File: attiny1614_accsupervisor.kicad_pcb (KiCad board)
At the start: 2 copper layers, 58 x 58 mm, 34 parts, among them J1 VXO7803-500-M-TR, J2 MSTBA_2,5_3-G, J3 Conn_01x02, J4 Conn_02x20_Odd_Even, J5 AVR-UPDI-6, K1 JSM1-12V-5, Q1 BC817, Q2 BC817, Q3 BC817, Q4 BSS84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

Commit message: r01 gerber generated
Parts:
- moved Q3 77.1 mm to (222.5, 91.5)
- moved R5 74.8 mm to (225.5, 89.5), turned to 90 degrees
- moved R3 73.2 mm to (214.0, 90.0), turned to 90 degrees
- moved R7 71.9 mm to (223.0, 84.5)
- moved R8 71.1 mm to (218.5, 72.5), turned to 90 degrees
- moved R10 66.6 mm to (218.5, 78.0), turned to 90 degrees
- moved R2 65.7 mm to (214.0, 79.5), turned to 270 degrees
- moved R9 59.5 mm to (218.5, 86.0), turned to 90 degrees
- moved R11 57.8 mm to (218.5, 91.5), turned to 90 degrees
- moved Q5 52.2 mm to (222.5, 87.5)
- moved F1 19.7 mm to (226.0, 52.5), turned to 180 degrees
- moved R12 17.2 mm to (240.5, 92.0)
- moved R13 17.2 mm to (243.5, 92.0)
- moved R14 17.2 mm to (234.5, 92.0)
- moved R15 17.2 mm to (237.5, 92.0)
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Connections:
- U1 pad 12: (no net) -> /ADC_ON
- U1 pad 4: /ADC1_VIN -> /ADC2_ACC
- U1 pad 5: /ADC2_ACC -> /ADC1_VIN
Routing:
- net /12V: track 0.00 -> 76.9 mm
- net /AVR_TX: track 0.00 -> 52.0 mm
- net /AVR_RX: track 0.00 -> 44.0 mm
- net /ADC1_VIN: track 0.00 -> 29.5 mm
- net /RLY_ON: track 0.00 -> 26.3 mm
- net /3V3: track 0.00 -> 24.5 mm
- net /ACC: track 0.00 -> 24.1 mm
- net /JST_TX: track 0.00 -> 21.2 mm
- net /12V_IN: track 0.00 -> 20.3 mm
- net /ADC2_ACC: track 0.00 -> 17.7 mm
- net /UPDI_DATA: track 0.00 -> 16.0 mm
- net Net-(D1-Pad2): track 0.00 -> 15.9 mm
- net /ADC_ON: track 0.00 -> 12.8 mm
- net /JST_RX: track 0.00 -> 10.9 mm
- net Net-(Q3-Pad1): track 0.00 -> 7.90 mm
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- added copper zone on B.Cu, net GND
- added copper zone on F.Cu, net GND

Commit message: Layout done
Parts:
- added G***: LOGO, attiny1614_accsupervisor:Doge, F.Cu at (230.0, 69.0)
- moved R13 48.4 mm to (197.5, 77.0), turned to 0 degrees
- moved J4 48.3 mm to (194.9, 99.2), turned to 90 degrees
- moved R14 39.1 mm to (197.5, 79.5), turned to 0 degrees
- moved R12 33.5 mm to (207.0, 92.0)
- moved R15 33.0 mm to (204.5, 92.0)
- moved U1 7.76 mm to (205.0, 81.5)
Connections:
- U1 pad 11: /RLY_ON -> /ADC1_VIN
- U1 pad 12: /ADC_ON -> /ADC2_ACC
- U1 pad 13: (no net) -> /ADC_ON
- U1 pad 4: /ADC2_ACC -> (no net)
- U1 pad 5: /ADC1_VIN -> (no net)
- U1 pad 8: (no net) -> /RLY_ON
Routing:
- net /AVR_TX: track 52.0 -> 19.1 mm
- net /AVR_RX: track 44.0 -> 16.7 mm
- net /RLY_ON: track 26.3 -> 9.89 mm
- net /JST_TX: track 21.2 -> 35.1 mm
- net /ADC1_VIN: track 29.5 -> 18.0 mm
- net /UPDI_DATA: track 16.0 -> 24.4 mm
- net /ADC2_ACC: track 17.7 -> 23.0 mm
- net /JST_RX: track 10.9 -> 5.86 mm
- net /3V3: track 24.5 -> 29.5 mm
- net /ADC_ON: track 12.8 -> 15.4 mm
- net GND: vias 90 -> 116
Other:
- board text added: "ACC Supervisor ATTINY r01 (c) 2020, Jason Kwon"

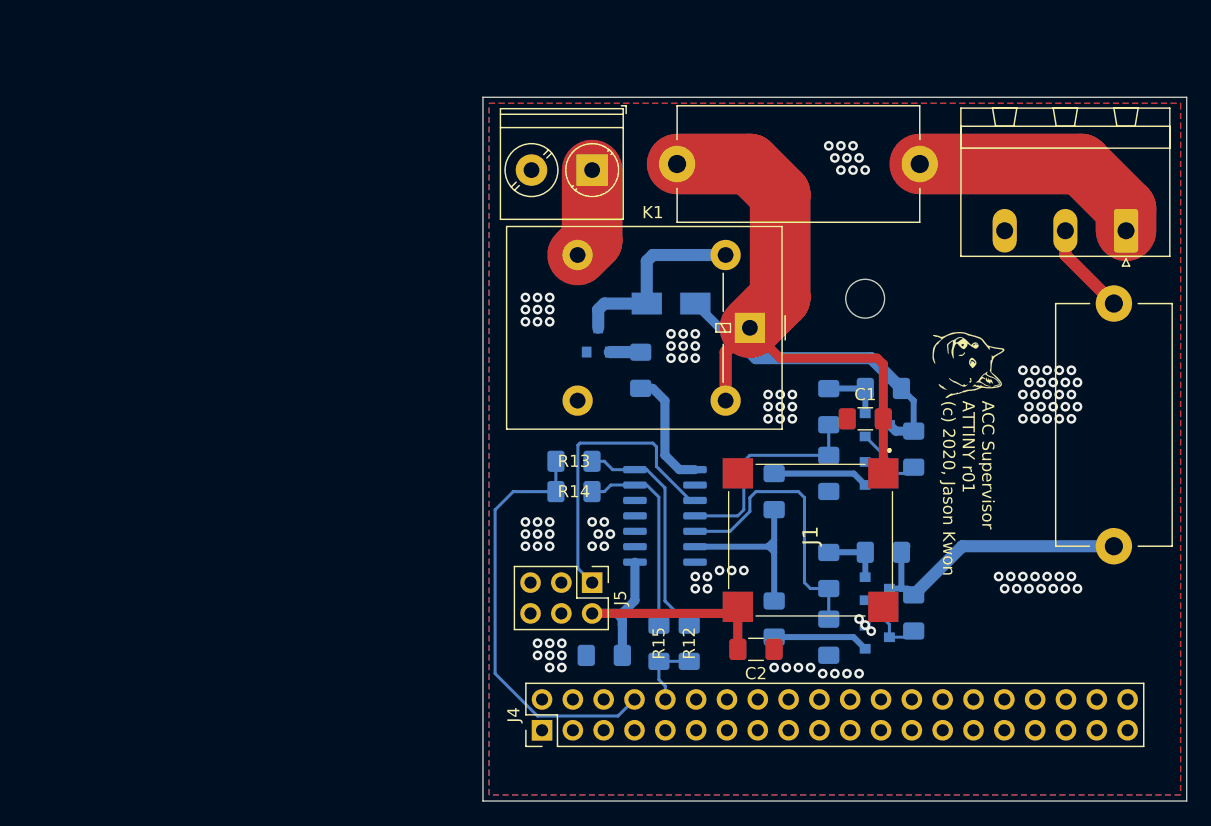
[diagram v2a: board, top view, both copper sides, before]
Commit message: BOM consolidation, 10/22uF to 4.7uFs
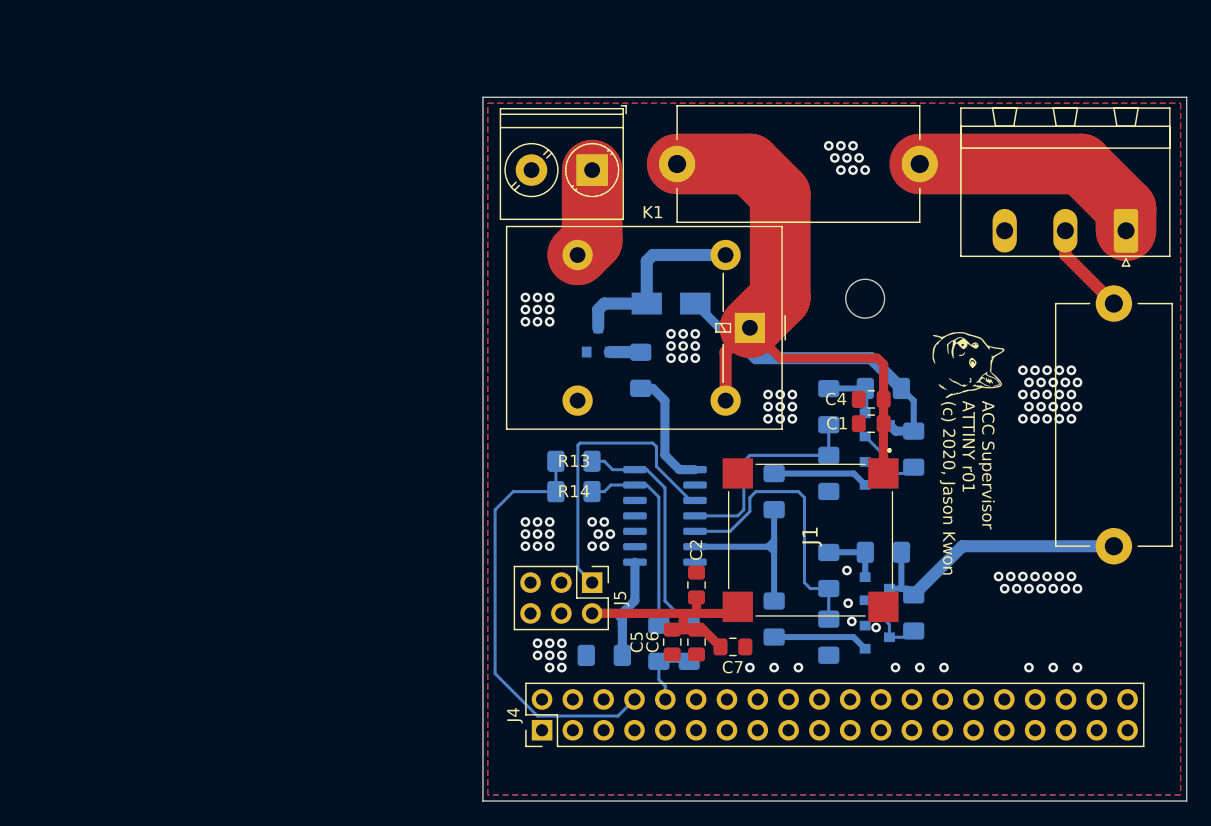
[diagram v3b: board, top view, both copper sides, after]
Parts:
- added C4: 4.7u, Capacitor_SMD:C_0805_2012Metric_Pad1.15x1.40mm_HandSolder, F.Cu at (222.0, 71.9)
- added C5: 4.7u, Capacitor_SMD:C_0805_2012Metric_Pad1.15x1.40mm_HandSolder, F.Cu at (205.6, 91.9)
- added C6: 4.7u, Capacitor_SMD:C_0805_2012Metric_Pad1.15x1.40mm_HandSolder, F.Cu at (207.6, 91.9)
- added C7: 4.7u, Capacitor_SMD:C_0805_2012Metric_Pad1.15x1.40mm_HandSolder, F.Cu at (210.6, 92.3)
- C1: value 10u -> 4.7u; footprint Capacitor_SMD:C_1206_3216Metric_Pad1.42x1.75mm_HandSolder -> Capacitor_SMD:C_0805_2012Metric_Pad1.15x1.40mm_HandSolder
- C2: value 22u -> 4.7u; footprint Capacitor_SMD:C_1206_3216Metric_Pad1.42x1.75mm_HandSolder -> Capacitor_SMD:C_0805_2012Metric_Pad1.15x1.40mm_HandSolder
- R1: value 1K -> 1k
- moved C2 7.22 mm to (207.6, 87.2), turned to 90 degrees
- moved C1 0.63 mm to (222.0, 73.9)
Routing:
- net /3V3: track 29.5 -> 35.4 mm
- net GND: vias 116 -> 111

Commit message: Gerber generated, r01
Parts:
- removed G***: LOGO, attiny1614_accsupervisor:Doge

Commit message: Doge silk
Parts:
- added G***: LOGO, attiny1614_accsupervisor:Doge, F.Cu at (230.0, 69.0)

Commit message: Q4, Q5 PFETs pin swap fixed
P ch. MOSFETs drain-source swapped pins are now fixed
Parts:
- turned Q4 to 270 degrees
- turned Q5 to 270 degrees
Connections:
- J1 pad 4: (no net) -> Net-(J1-Pad4)
- J4 pad 1: (no net) -> Net-(J4-Pad1)
- J4 pad 11: (no net) -> Net-(J4-Pad11)
- J4 pad 12: (no net) -> Net-(J4-Pad12)
- J4 pad 13: (no net) -> Net-(J4-Pad13)
- J4 pad 15: (no net) -> Net-(J4-Pad15)
- J4 pad 16: (no net) -> Net-(J4-Pad16)
- J4 pad 17: (no net) -> Net-(J4-Pad17)
- J4 pad 18: (no net) -> Net-(J4-Pad18)
- J4 pad 19: (no net) -> Net-(J4-Pad19)
- J4 pad 2: (no net) -> Net-(J4-Pad2)
- J4 pad 21: (no net) -> Net-(J4-Pad21)
- J4 pad 22: (no net) -> Net-(J4-Pad22)
- J4 pad 23: (no net) -> Net-(J4-Pad23)
- J4 pad 24: (no net) -> Net-(J4-Pad24)
- J4 pad 26: (no net) -> Net-(J4-Pad26)
- J4 pad 27: (no net) -> Net-(J4-Pad27)
- J4 pad 28: (no net) -> Net-(J4-Pad28)
- J4 pad 29: (no net) -> Net-(J4-Pad29)
- J4 pad 3: (no net) -> Net-(J4-Pad3)
- J4 pad 31: (no net) -> Net-(J4-Pad31)
- J4 pad 32: (no net) -> Net-(J4-Pad32)
- J4 pad 33: (no net) -> Net-(J4-Pad33)
- J4 pad 35: (no net) -> Net-(J4-Pad35)
- J4 pad 36: (no net) -> Net-(J4-Pad36)
- J4 pad 37: (no net) -> Net-(J4-Pad37)
- J4 pad 38: (no net) -> Net-(J4-Pad38)
- J4 pad 4: (no net) -> Net-(J4-Pad4)
- J4 pad 40: (no net) -> Net-(J4-Pad40)
- J4 pad 5: (no net) -> Net-(J4-Pad5)
- J4 pad 7: (no net) -> Net-(J4-Pad7)
- J5 pad 3: (no net) -> Net-(J5-Pad3)
- J5 pad 4: (no net) -> Net-(J5-Pad4)
- J5 pad 5: (no net) -> Net-(J5-Pad5)
- K1 pad 4: (no net) -> Net-(K1-Pad4)
- Q4 pad 2: Net-(Q4-Pad2) -> /12V
- Q4 pad 3: /12V -> Net-(Q4-Pad3)
- Q5 pad 2: Net-(Q5-Pad2) -> /ACC
- Q5 pad 3: /ACC -> Net-(Q5-Pad3)
- R6 pad 1: Net-(Q4-Pad2) -> Net-(Q4-Pad3)
- R7 pad 1: Net-(Q5-Pad2) -> Net-(Q5-Pad3)
- R8 pad 2: Net-(Q4-Pad2) -> Net-(Q4-Pad3)
- R9 pad 2: Net-(Q5-Pad2) -> Net-(Q5-Pad3)
- U1 pad 2: (no net) -> Net-(U1-Pad2)
- U1 pad 3: (no net) -> Net-(U1-Pad3)
- U1 pad 4: (no net) -> Net-(U1-Pad4)
- U1 pad 5: (no net) -> Net-(U1-Pad5)
- U1 pad 9: (no net) -> Net-(U1-Pad9)
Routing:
- net Net-(Q5-Pad3): track 0.00 -> 7.44 mm
- net Net-(Q4-Pad3): track 0.00 -> 7.43 mm
- net Net-(Q5-Pad2): track 5.09 -> 0.00 mm
- net Net-(Q4-Pad2): track 5.07 -> 0.00 mm
- net Net-(Q3-Pad3): track 6.09 -> 8.04 mm
- net Net-(Q2-Pad3): track 6.09 -> 8.02 mm
- net /12V: track 76.9 -> 77.9 mm
- net /ACC: track 24.1 -> 23.4 mm
- net GND: vias 111 -> 110

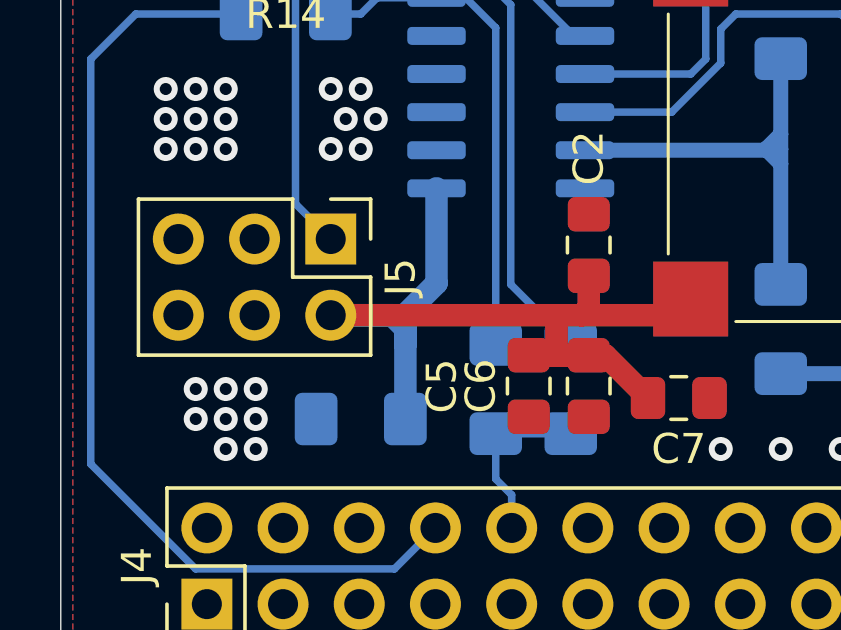
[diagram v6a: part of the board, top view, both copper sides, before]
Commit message: UPDI_DATA/~RESET pullup added
10k pullup for UPDI_DATA/~RESET pin added
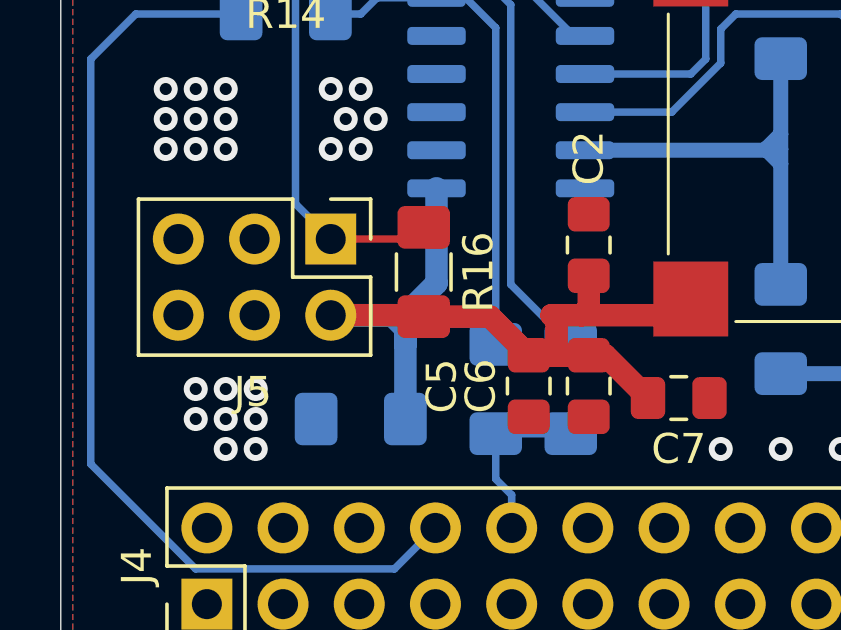
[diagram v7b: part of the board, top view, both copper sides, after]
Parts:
- added R16: 10k, Resistor_SMD:R_1206_3216Metric_Pad1.42x1.75mm_HandSolder, F.Cu at (202.1, 88.1)
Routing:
- net /UPDI_DATA: track 24.4 -> 27.7 mm
